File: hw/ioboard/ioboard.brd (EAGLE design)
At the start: 113.7 x 40.6 mm, 33 parts, among them IC1 MAX232, M1 ENC_MODULE, X2 2540-

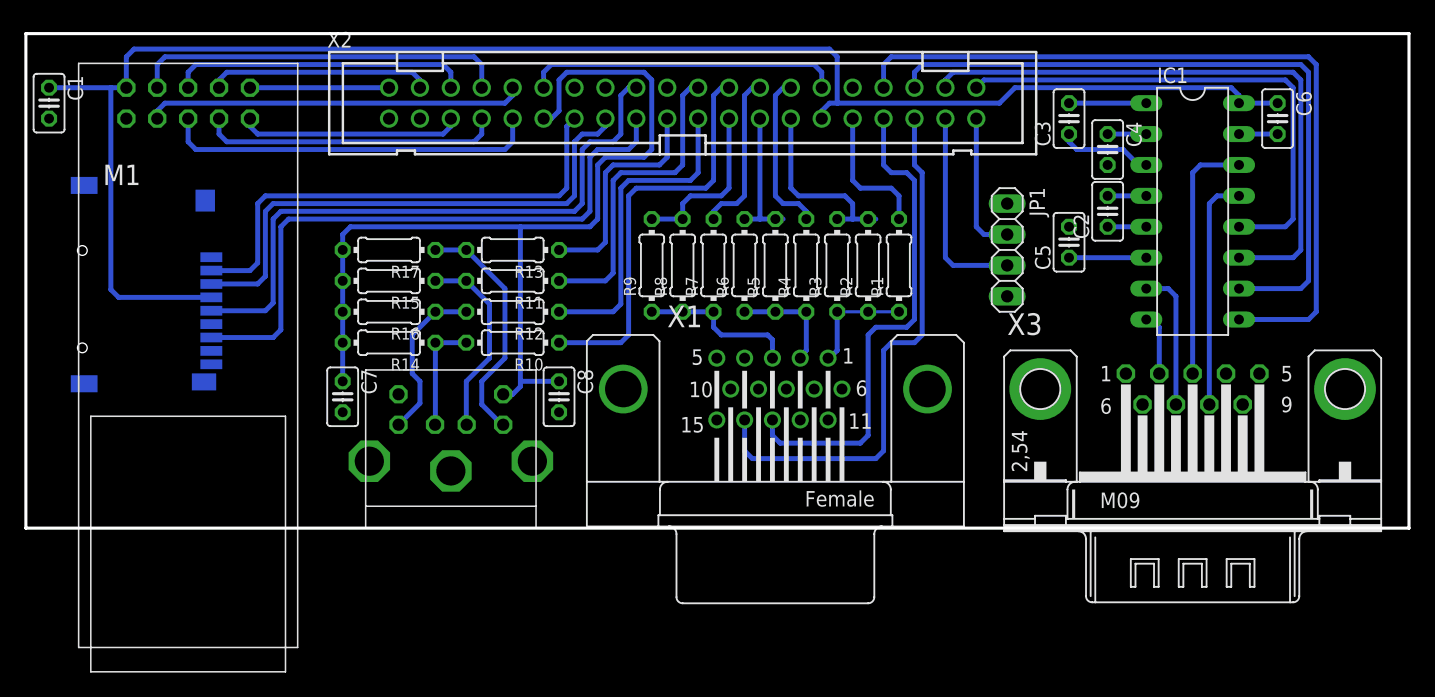
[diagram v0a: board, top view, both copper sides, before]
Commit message: New version of IO board - fix issue #2 but remove SD card and ethernet ... not need at this time anyway
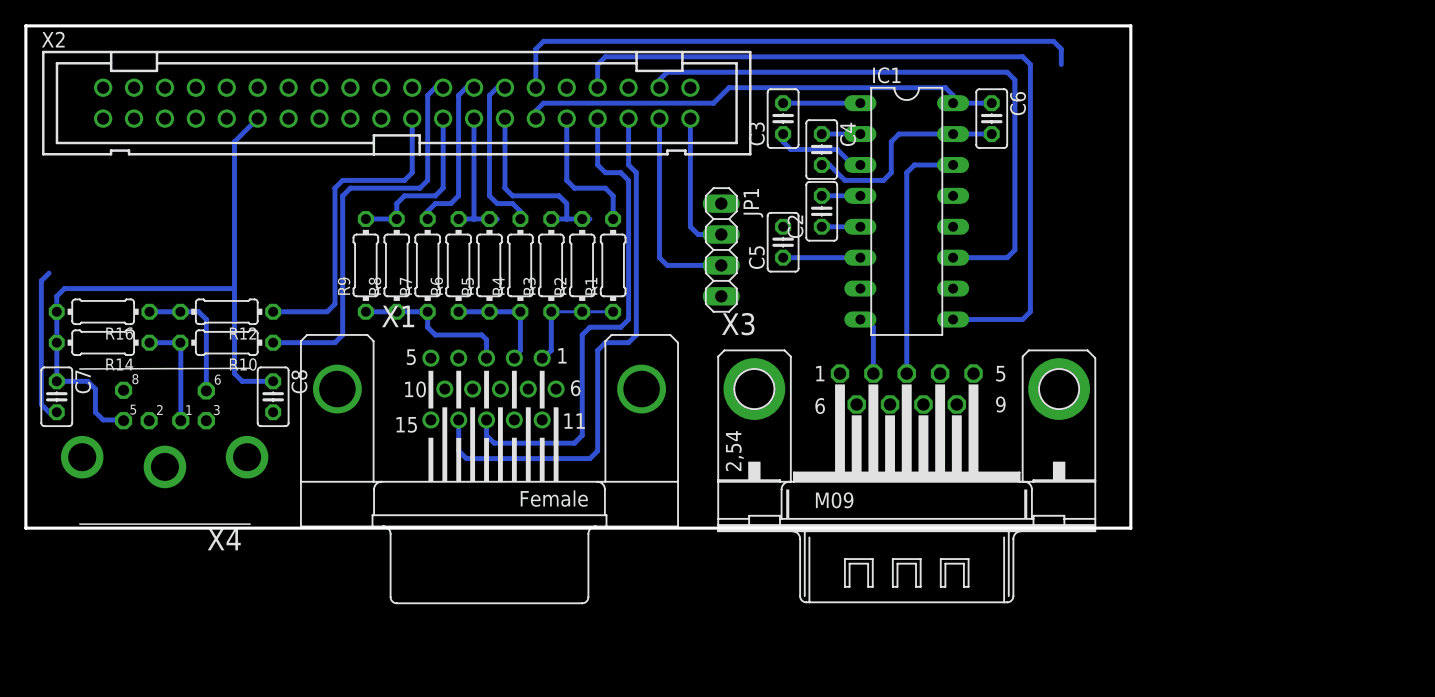
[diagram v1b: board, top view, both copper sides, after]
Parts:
- removed C1: 100nF, rcl:C025-025X050
- removed M1: ENC_MODULE, VladisLib:ENC28J60-MODULE
- removed R11, R13: 120, rcl:0204/7
- removed R15, R17: 2k2, rcl:0204/7
- removed U$1: MINIDIN_6, VladisLib:MINIDIN_6_3GND
- removed U$2: MICROSD_PP, DE1594-v2:MICROSD_PP
- added X4: (no value), mini_din:M_DIN6
- moved C2 23.5 mm to (65.4, 26.0)
- moved C4 23.5 mm to (65.4, 31.1)
- moved C6 23.5 mm to (79.4, 33.7)
- moved IC1 23.5 mm to (72.4, 26.0)
- moved R2 23.5 mm to (45.7, 21.6)
- moved R4 23.5 mm to (40.6, 21.6)
- moved X3 23.5 mm to (72.4, 11.4)
- moved C7 23.5 mm to (2.54, 10.8)
- moved R10 23.5 mm to (16.5, 15.2)
- moved R12 23.5 mm to (16.5, 17.8)
- moved R8 23.5 mm to (30.5, 21.6)
- moved R9 23.5 mm to (27.9, 21.6)
- moved X2 23.5 mm to (30.5, 34.9)
- moved C3 23.5 mm to (62.2, 33.7)
- moved C5 23.5 mm to (62.2, 23.5)
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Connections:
- removed net CTS: IC1.13, X3.8
- removed net ENC_CLK: M1.P$1, X2.2
- removed net ENC_CS: M1.P$7, X2.8
- removed net ENC_INT: M1.P$2, X2.5
- removed net ENC_RES: M1.P$8, X2.10
- removed net ENC_SCK: M1.P$6, X2.9
- removed net ENC_SI: M1.P$5, X2.6
- removed net ENC_SO: M1.P$4, X2.7
- removed net ENC_WOL: M1.P$3, X2.4
- removed net MS_CLK: R13.1, X2.19
- removed net MS_DAT: R11.1, X2.22
- removed net N$3: R12.2, R16.1, U$1.5
- removed net N$4: R13.2, R17.1, U$1.6
- removed net RTS: IC1.7, X3.7
- removed net SD_CS: U$2.2, X2.13
- removed net SD_DI: U$2.3, X2.15
- removed net SD_DO: U$2.7, X2.17
- removed net SD_SCK: U$2.5, X2.18
- removed net UART1_CTS: IC1.12, X2.40
- removed net UART1_RTS: IC1.10, X2.36
- net +3V3: no longer C1.1, M1.P$9, U$2.4
- net +5V: now also X4.5; no longer R15.2, R17.2, U$1.4
- net GND: now also X4.3, X4.SH1, X4.SH2, X4.SH3; no longer C1.2, M1.P$10, U$1.3, U$1.CASE1, U$1.CASE2, U$1.SHIELDING, U$2.6, U$2.GND@1, U$2.GND@2, U$2.GND@3, U$2.GND@4
- net N$1: now also R12.2, R16.1, X4.6; no longer R10.2, R14.1, U$1.1
- net N$2: now also R10.2, R14.1, X4.1; no longer R11.2, R15.1, U$1.2
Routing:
- net +3V3: track 136.5 -> 39.8 mm
- net UART1_RTS: track 57.3 -> 0.00 mm
- net SD_DO: track 51.1 -> 0.00 mm
- net SD_SCK: track 51.0 -> 0.00 mm
- net GND: track 29.1 -> 78.3 mm
- net SD_DI: track 44.1 -> 0.00 mm
- net UART1_CTS: track 42.1 -> 0.00 mm
- net SD_CS: track 40.8 -> 0.00 mm
- net ENC_SCK: track 31.6 -> 0.00 mm
- net ENC_CS: track 31.0 -> 0.00 mm
- net ENC_RES: track 31.0 -> 0.00 mm
- net MS_DAT: track 25.8 -> 0.00 mm
- net ENC_SI: track 24.7 -> 0.00 mm
- net ENC_SO: track 24.7 -> 0.00 mm
- net +5V: track 78.9 -> 55.0 mm
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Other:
- board size 113.7 x 40.6 mm -> 90.8 x 41.3 mm
